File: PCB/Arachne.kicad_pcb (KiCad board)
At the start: 2 copper layers, 100 x 70 mm, 275 parts, among them J101 Salae_logic, J201 SW2, J301 SW2, J401 SW2, J501 SW2, J601 SW2, J701 SW2, J801 V_IN, J901 USB_B, J902 PROG_CONN_STM_6p, J903 DBG_UART, M201 Stepper_Motor_bipolar, M301 Stepper_Motor_bipolar, M401 Stepper_Motor_bipolar, M501 Stepper_Motor_bipolar, M601 Stepper_Motor_bipolar, M701 Stepper_Motor_bipolar, Q801 AOD4189, SW101 SW_Push, U101 STM32L452CEUx, U102 WS2818B, U201 L6470_HTSSOP28, U301 L6470_HTSSOP28, U401 L6470_HTSSOP28, U501 L6470_HTSSOP28, U601 L6470_HTSSOP28, U701 L6470_HTSSOP28, U801 ACS712xLCTR-20A, U802 NCP1117-5.0_SOT223, U803 L5973D, U804 NCP1117-3.3_SOT223, U901 USBLC6-2SC6

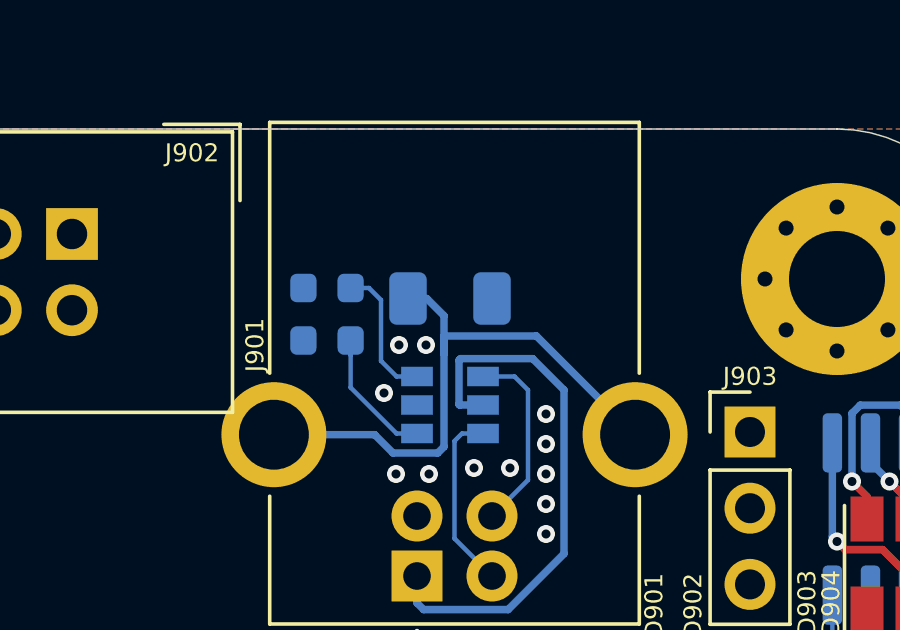
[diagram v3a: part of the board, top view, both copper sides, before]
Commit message: PCB: change package size of USB ferrite from 1206 to 0803
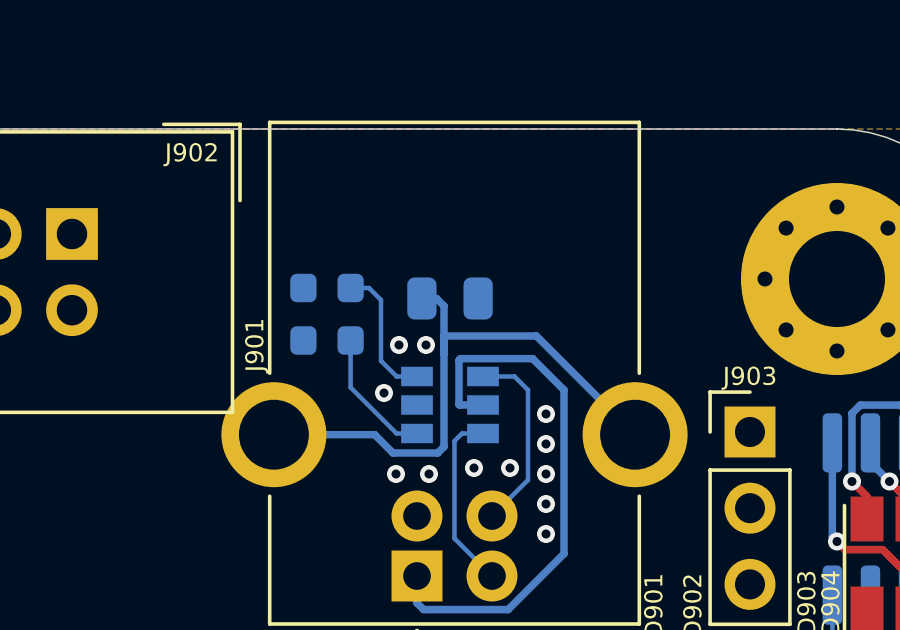
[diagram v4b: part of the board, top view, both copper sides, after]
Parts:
- L901: footprint Inductor_SMD:L_1206_3216Metric -> Inductor_SMD:L_0805_2012Metric
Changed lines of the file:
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@@
     (thickness 1.6)
     (drawings 35)
-    (tracks 2900)
+    (tracks 2901)
     (zones 0)
     (modules 275)
@@
   )
   (setup
-    (last_trace_width 0.15)
+    (last_trace_width 0.25)
     (user_trace_width 0.25)
     (user_trace_width 0.5)
@@
     (add_net "Net-(D801-Pad1)")
     (add_net "Net-(D801-Pad2)")
+    (add_net "Net-(D802-Pad3)")
+    (add_net "Net-(D802-Pad5)")
     (add_net "Net-(D803-Pad1)")
     (add_net "Net-(D805-Pad1)")
@@
     (add_net "Net-(D903-Pad1)")
     (add_net "Net-(D904-Pad1)")
+    (add_net "Net-(J101-Pad5)")
+    (add_net "Net-(J101-Pad6)")
+    (add_net "Net-(J101-Pad9)")
     (add_net "Net-(J801-Pad3)")
     (add_net "Net-(J901-Pad5)")
@@
     (add_net "Net-(R808-Pad2)")
     (add_net "Net-(R810-Pad1)")
+    (add_net "Net-(U101-Pad1)")
+    (add_net "Net-(U101-Pad11)")
+    (add_net "Net-(U101-Pad17)")
+    (add_net "Net-(U101-Pad29)")
+    (add_net "Net-(U101-Pad30)")
+    (add_net "Net-(U101-Pad31)")
+    (add_net "Net-(U101-Pad38)")
+    (add_net "Net-(U102-Pad4)")
+    (add_net "Net-(U201-Pad25)")
+    (add_net "Net-(U201-Pad7)")
+    (add_net "Net-(U201-Pad8)")
+    (add_net "Net-(U301-Pad25)")
+    (add_net "Net-(U301-Pad7)")
+    (add_net "Net-(U301-Pad8)")
+    (add_net "Net-(U401-Pad25)")
+    (add_net "Net-(U401-Pad7)")
+    (add_net "Net-(U401-Pad8)")
+    (add_net "Net-(U501-Pad25)")
+    (add_net "Net-(U501-Pad7)")
+    (add_net "Net-(U501-Pad8)")
+    (add_net "Net-(U601-Pad25)")
+    (add_net "Net-(U601-Pad7)")
+    (add_net "Net-(U601-Pad8)")
+    (add_net "Net-(U701-Pad25)")
+    (add_net "Net-(U701-Pad7)")
+    (add_net "Net-(U701-Pad8)")
+    (add_net "Net-(U803-Pad2)")
+    (add_net "Net-(U803-Pad6)")
     (add_net USB_VCC)
     (add_net VMOT)
   )
+  (module Inductor_SMD:L_0805_2012Metric (layer B.Cu)
+    (at 182.1 85.65)
+    (descr "Inductor SMD 0805 (2012 Metric), square (rectangular) end terminal, IPC_7351 nominal, (Body size source: https://docs.google.com/spreadsheets/d/1BsfQQcO9C6DZCsRaXUlFlo91Tg2WpOkGARC1WS5S8t0/edit?usp=sharing), generated with kicad-footprint-generator")
+    (tags inductor)
+    (attr smd)
+    (fp_text reference L901 (at 0 1.65) (layer B.SilkS)
+      (effects (font (size 1 1) (thickness 0.15)) (justify mirror))
+    )
+    (fp_text value "50R@100MHz, 3A" (at 0 -1.65) (layer B.Fab)
+      (effects (font (size 1 1) (thickness 0.15)) (justify mirror))
+    )
+    (fp_text user %R (at 0 0) (layer B.Fab)
+      (effects (font (size 0.5 0.5) (thickness 0.08)) (justify mirror))
+    )
+    (fp_line (start 1.68 -0.95) (end -1.68 -0.95) (layer B.CrtYd) (width 0.05))
+    (fp_line (start 1.68 0.95) (end 1.68 -0.95) (layer B.CrtYd) (width 0.05))
+    (fp_line (start -1.68 0.95) (end 1.68 0.95) (layer B.CrtYd) (width 0.05))
+    (fp_line (start -1.68 -0.95) (end -1.68 0.95) (layer B.CrtYd) (width 0.05))
+    (fp_line (start -0.258578 -0.71) (end 0.258578 -0.71) (layer B.SilkS) (width 0.12))
+    (fp_line (start -0.258578 0.71) (end 0.258578 0.71) (layer B.SilkS) (width 0.12))
+    (fp_line (start 1 -0.6) (end -1 -0.6) (layer B.Fab) (width 0.1))
+    (fp_line (start 1 0.6) (end 1 -0.6) (layer B.Fab) (width 0.1))
+    (fp_line (start -1 0.6) (end 1 0.6) (layer B.Fab) (width 0.1))
+    (fp_line (start -1 -0.6) (end -1 0.6) (layer B.Fab) (width 0.1))
+    (pad 2 smd roundrect (at 0.9375 0) (size 0.975 1.4) (layers B.Cu B.Paste B.Mask) (roundrect_rratio 0.25)
+      (net 1 GND))
+    (pad 1 smd roundrect (at -0.9375 0) (size 0.975 1.4) (layers B.Cu B.Paste B.Mask) (roundrect_rratio 0.25)
+      (net 93 "Net-(J901-Pad5)"))
+    (model ${KISYS3DMOD}/Inductor_SMD.3dshapes/L_0805_2012Metric.wrl
+      (at (xyz 0 0 0))
+      (scale (xyz 1 1 1))
+      (rotate (xyz 0 0 0))
+    )
+  )
   (module TestPoint:TestPoint_THTPad_D1.0mm_Drill0.5mm (layer F.Cu)
     (at 102.25 88.5 90)
@@
     )
   )
-  (module Inductor_SMD:L_1206_3216Metric (layer B.Cu)
-    (at 182.1 85.65)
-    (descr "Inductor SMD 1206 (3216 Metric), square (rectangular) end terminal, IPC_7351 nominal, (Body size source: http://www.tortai-tech.com/upload/download/2011102023233369053.pdf), generated with kicad-footprint-generator")
-    (tags inductor)
-    (attr smd)
-    (fp_text reference L901 (at 0 -1.45) (layer B.SilkS)
-      (effects (font (size 0.6 0.6) (thickness 0.1)) (justify mirror))
-    )
-    (fp_text value "50R@100MHz, 3A" (at 0 -1.82) (layer B.Fab)
-      (effects (font (size 1 1) (thickness 0.15)) (justify mirror))
-    )
-    (fp_text user %R (at 0 0) (layer B.Fab)
-      (effects (font (size 0.6 0.6) (thickness 0.1)) (justify mirror))
-    )
-    (fp_line (start 2.28 -1.12) (end -2.28 -1.12) (layer B.CrtYd) (width 0.05))
-    (fp_line (start 2.28 1.12) (end 2.28 -1.12) (layer B.CrtYd) (width 0.05))
-    (fp_line (start -2.28 1.12) (end 2.28 1.12) (layer B.CrtYd) (width 0.05))
-    (fp_line (start -2.28 -1.12) (end -2.28 1.12) (layer B.CrtYd) (width 0.05))
-    (fp_line (start -0.602064 -0.91) (end 0.602064 -0.91) (layer B.SilkS) (width 0.12))
-    (fp_line (start -0.602064 0.91) (end 0.602064 0.91) (layer B.SilkS) (width 0.12))
-    (fp_line (start 1.6 -0.8) (end -1.6 -0.8) (layer B.Fab) (width 0.1))
-    (fp_line (start 1.6 0.8) (end 1.6 -0.8) (layer B.Fab) (width 0.1))
-    (fp_line (start -1.6 0.8) (end 1.6 0.8) (layer B.Fab) (width 0.1))
-    (fp_line (start -1.6 -0.8) (end -1.6 0.8) (layer B.Fab) (width 0.1))
-    (pad 2 smd roundrect (at 1.4 0) (size 1.25 1.75) (layers B.Cu B.Paste B.Mask) (roundrect_rratio 0.2)
-      (net 1 GND))
-    (pad 1 smd roundrect (at -1.4 0) (size 1.25 1.75) (layers B.Cu B.Paste B.Mask) (roundrect_rratio 0.2)
-      (net 93 "Net-(J901-Pad5)"))
-    (model ${KISYS3DMOD}/Inductor_SMD.3dshapes/L_1206_3216Metric.wrl
-      (at (xyz 0 0 0))
-      (scale (xyz 1 1 1))
-      (rotate (xyz 0 0 0))
-    )
-  )
   (module Package_TO_SOT_SMD:TO-252-2 (layer F.Cu)
     (at 111.4 93.8)
@@
   (segment (start 184.7 91.7) (end 184.7 88.7) (width 0.15) (layer B.Cu) (net 92))
   (segment (start 179.59 90.19) (end 176.23 90.19) (width 0.25) (layer B.Cu) (net 93))
-  (segment (start 180.7 85.65) (end 181.325 85.65) (width 0.25) (layer B.Cu) (net 93))
-  (segment (start 181.325 85.65) (end 181.9 86.225) (width 0.25) (layer B.Cu) (net 93))
   (segment (start 181.9 90.591002) (end 181.691002 90.8) (width 0.25) (layer B.Cu) (net 93))
   (segment (start 181.691002 90.8) (end 180.2 90.8) (width 0.25) (layer B.Cu) (net 93))
   (segment (start 180.2 90.8) (end 179.59 90.19) (width 0.25) (layer B.Cu) (net 93))
-  (segment (start 181.9 86.225) (end 181.9 87.5) (width 0.25) (layer B.Cu) (net 93))
   (segment (start 181.9 87.5) (end 181.9 90.591002) (width 0.25) (layer B.Cu) (net 93))
   (segment (start 181.9 86.9) (end 181.9 87.5) (width 0.25) (layer B.Cu) (net 93))
   (segment (start 188.27 90.19) (end 184.98 86.9) (width 0.25) (layer B.Cu) (net 93))
   (segment (start 184.98 86.9) (end 181.9 86.9) (width 0.25) (layer B.Cu) (net 93))
+  (segment (start 181.1 85.7) (end 181.375 85.7) (width 0.25) (layer B.Cu) (net 93))
+  (segment (start 181.65 85.65) (end 181.1625 85.65) (width 0.25) (layer B.Cu) (net 93))
+  (segment (start 181.9 87.5) (end 181.9 85.9) (width 0.25) (layer B.Cu) (net 93))
+  (segment (start 181.9 85.9) (end 181.65 85.65) (width 0.25) (layer B.Cu) (net 93))
   (segment (start 198.655 96.955) (end 198.655 95.5375) (width 0.15) (layer B.Cu) (net 98))
   (segment (start 198.75 97.05) (end 198.655 96.955) (width 0.15) (layer B.Cu) (net 98))

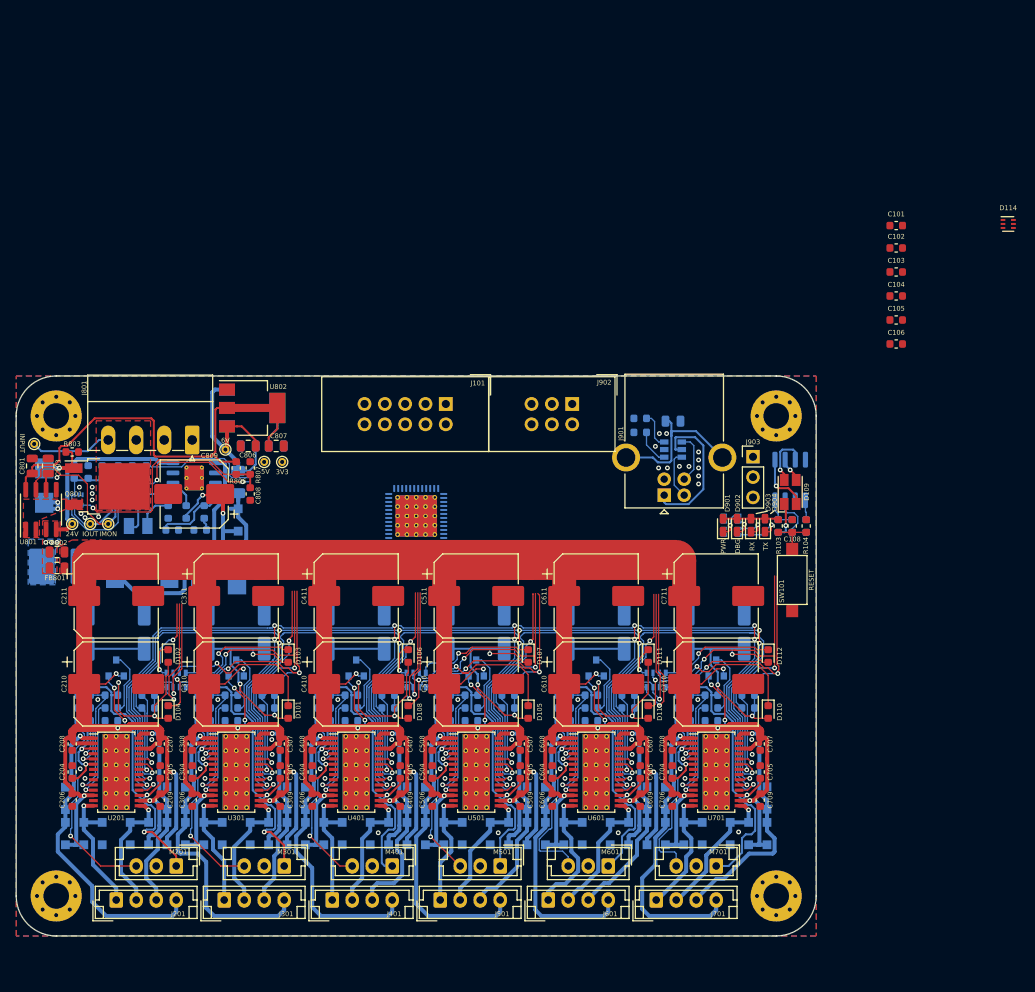
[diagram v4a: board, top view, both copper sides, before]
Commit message: Schema & PCB: add routing of MCu connection, debug and extension port
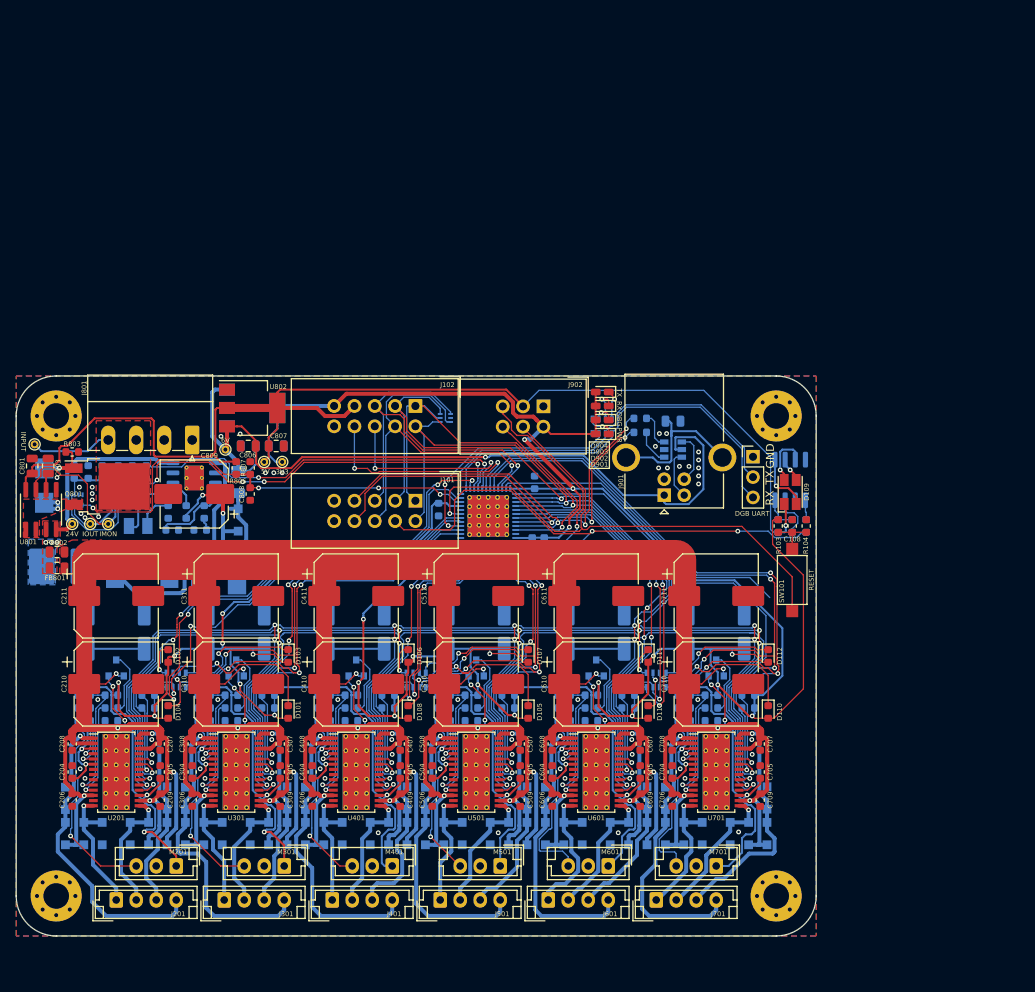
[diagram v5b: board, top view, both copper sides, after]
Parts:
- added J102: Extension, Connector_IDC:IDC-Header_2x05_P2.54mm_Vertical, F.Cu at (149.9, 83.8)
- C101, C102, C103, C104, C105, C106, D114: moved to B.Cu
- moved D114 74.4 mm to (153.7, 85.2), turned to 180 degrees
- moved C101 67.3 mm to (152.8, 96.7), turned to 270 degrees
- moved C106 63.3 mm to (152.9, 103.4), turned to 270 degrees
- moved C105 63.3 mm to (154.5, 103.4), turned to 270 degrees
- moved C103 55.6 mm to (166.0, 101.0), turned to 270 degrees
- moved C104 55.1 mm to (164.5, 101.0), turned to 270 degrees
- moved C102 53.9 mm to (164.8, 93.3), turned to 90 degrees
- moved D904 26.3 mm to (173.2, 82.0), turned to 180 degrees
- moved D903 23.8 mm to (173.2, 83.8), turned to 180 degrees
- moved D902 21.4 mm to (173.2, 85.5), turned to 180 degrees
- moved RN901 20.3 mm to (173.2, 86.2), turned to 270 degrees
- moved D901 18.9 mm to (173.2, 87.2), turned to 180 degrees
- moved J101 12.7 mm to (149.9, 95.6)
- moved U101 9.00 mm to (159.0, 97.5)
- moved J902 3.61 mm to (165.9, 83.8)
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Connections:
- D114 pad 1: /UART_2_RX -> /I2C_SDA
- D114 pad 3: /UART_2_TX -> /I2C_SCL
- J101 pad 5: (no net) -> /I2C_SDA
- J101 pad 6: (no net) -> /I2C_SCL
- RN901 pad 5: /UART_2_TX -> /UART_2_RX
- RN901 pad 6: /UART_2_RX -> /UART_2_TX
- U101 pad 11: (no net) -> /FLAG_1
- U101 pad 14: /BUSY_6 -> /CS_1
- U101 pad 17: (no net) -> /EXT_1
- U101 pad 18: /FLAG_1 -> /EXT_2
- U101 pad 19: /FLAG_2 -> /FLAG_6
- U101 pad 2: /BUSY_4 -> /FLAG_2
- U101 pad 20: /FLAG_3 -> /BUSY_6
- U101 pad 21: /CS_4 -> /I2C_SCL
- U101 pad 22: /CS_5 -> /I2C_SDA
- U101 pad 29: (no net) -> /FLAG_5
- U101 pad 3: /BUSY_5 -> /BUSY_2
- U101 pad 30: (no net) -> /BUSY_5
- U101 pad 31: (no net) -> /CS_5
- U101 pad 39: /FLAG_4 -> (no net)
- U101 pad 41: /FLAG_5 -> /FLAG_4
- U101 pad 42: /FLAG_6 -> /BUSY_4
- U101 pad 43: /CS_1 -> /CS_4
- U101 pad 45: /CS_2 -> /FLAG_3
- U101 pad 5: /BUSY_1 -> /CS_2
- U101 pad 6: /BUSY_2 -> /BUSY_1
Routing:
- net +3V3: track 529.3 -> 780.2 mm, vias 35 -> 44
- net +5V: track 60.9 -> 152.7 mm
- net /SPI_SCK: track 212.2 -> 291.4 mm, vias 16 -> 18
- net /SPI_MOSI: track 212.2 -> 285.2 mm, vias 6 -> 9
- net /RESET: track 0.00 -> 73.0 mm, vias 0 -> 1
- net /RGB_STAT: track 0.00 -> 72.9 mm, vias 0 -> 2
- net /SPI_MISO: track 241.3 -> 312.8 mm, vias 16 -> 17
- net USB_VCC: track 44.3 -> 100.5 mm, vias 0 -> 1
- net /USB_D+: track 0.00 -> 55.0 mm, vias 0 -> 3
- net /USB_D-: track 0.00 -> 54.7 mm, vias 0 -> 3
- net /UART_2_RX: track 0.00 -> 50.0 mm
- net /I2C_SDA: track 0.00 -> 49.7 mm, vias 0 -> 1
- net /UART_2_TX: track 0.00 -> 49.1 mm
- net /I2C_SCL: track 0.00 -> 47.2 mm, vias 0 -> 1
- net /CS_1: track 27.7 -> 73.5 mm, vias 2 -> 5
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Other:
- board text added: "DGB UART"
- board text added: "GND"

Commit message: PCB: add ground via stitching, fix unconnected items
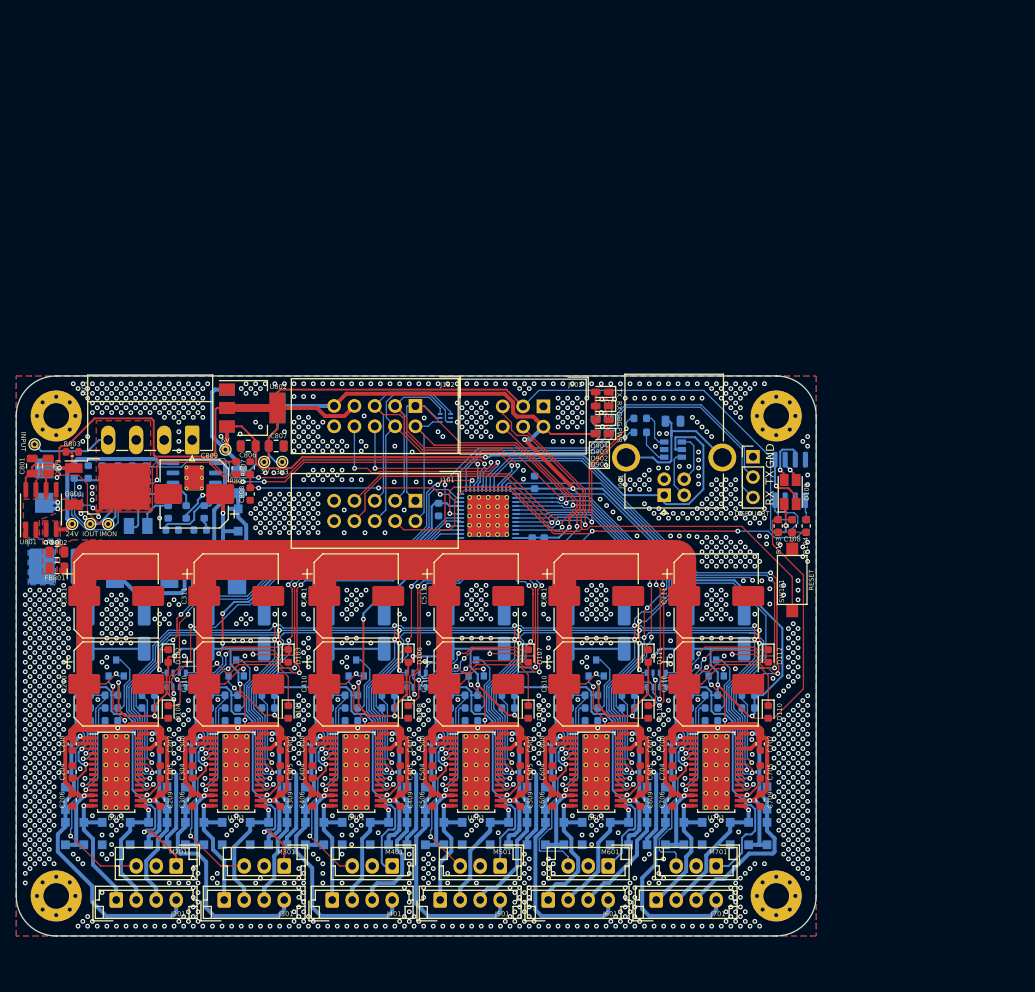
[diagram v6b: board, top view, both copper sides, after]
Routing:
- net GND: track 39.4 -> 36.4 mm, vias 59 -> 1550
- net /SPI_MOSI: track 285.2 -> 284.5 mm
- net /SPI_MISO: track 312.8 -> 312.1 mm
- net /SPI_SCK: track 291.4 -> 290.7 mm
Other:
- board text added: "DGB-UART"
- board text removed: "DGB UART"
